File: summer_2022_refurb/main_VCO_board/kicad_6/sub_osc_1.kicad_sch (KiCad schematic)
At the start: 4 parts, among them SW601 SW_DPDT_CO, SW602 SR1712F-0204

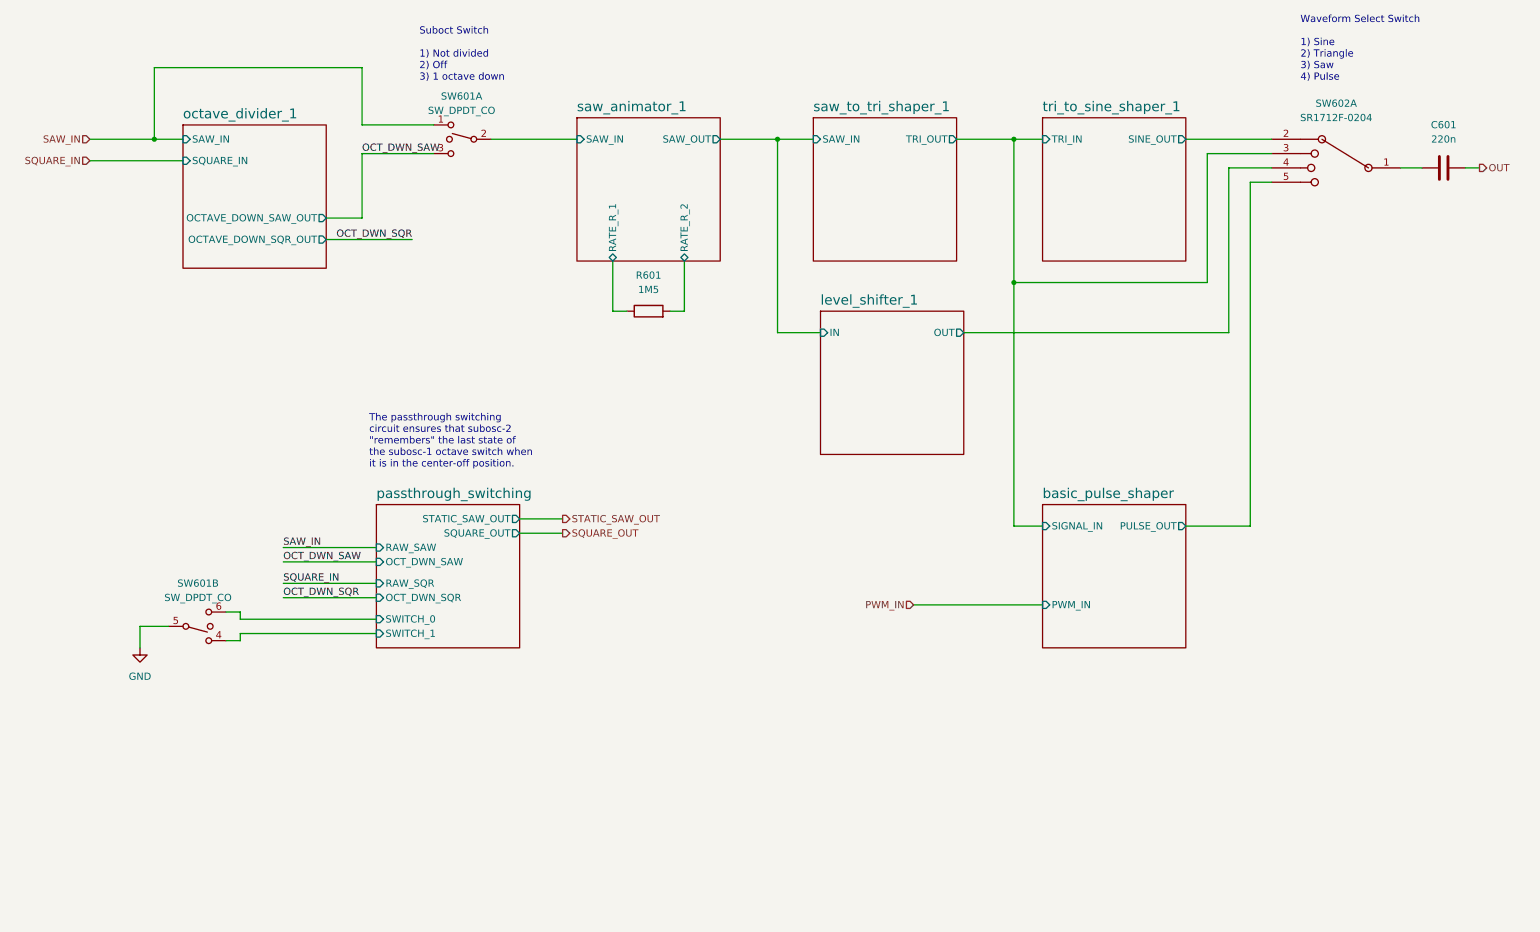
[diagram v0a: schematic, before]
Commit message: Fix VCO issues, suboct switching, component values
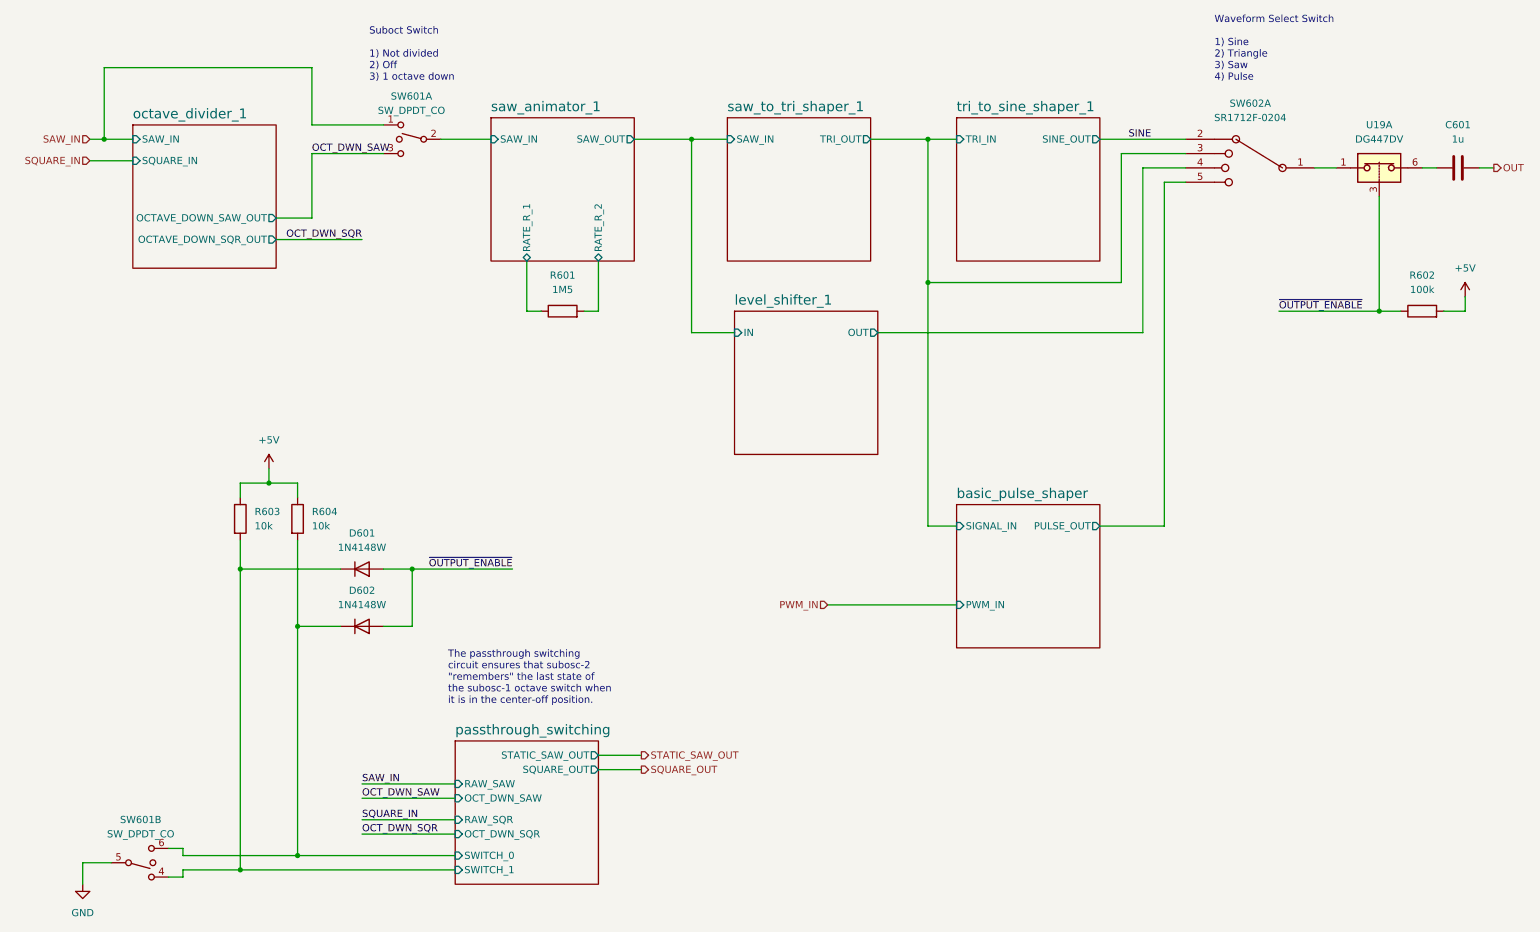
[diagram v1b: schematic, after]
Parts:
- added D601, D602: 1N4148W, Diode_SMD:D_SOD-123, symbol Diode:1N4148W
- added R602: 100k, Resistor_SMD:R_0805_2012Metric, symbol Device:R
- added R603, R604: 10k, Resistor_SMD:R_0805_2012Metric, symbol Device:R
- added U19: DG447DV, Package_SO:TSOP-6_1.65x3.05mm_P0.95mm, symbol custom_symbols:DG447DV
- C601: value 220n -> 1u; footprint Capacitor_THT:C_Rect_L7.0mm_W2.5mm_P5.00mm -> Capacitor_THT:C_Rect_L7.2mm_W5.5mm_P5.00mm_FKS2_FKP2_MKS2_MKP2
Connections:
- net passthrough_switching/SWITCH_0: now also D602.1 (K), R604.2
- net passthrough_switching/SWITCH_1: now also D601.1 (K), R603.2
- net at SW602.1: now also U19.1; no longer C601.1
- net tri_to_sine_shaper_1/SINE_OUT renamed SINE
- new net: C601.1, U19.6
- new net +5V: R602.2, R603.1, R604.1
- new net ~{OUTPUT_ENABLE}: D601.2 (A), D602.2 (A), R602.1, U19.3
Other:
- moved on the sheet: C601, R601, SW601A, SW601B, SW602A
